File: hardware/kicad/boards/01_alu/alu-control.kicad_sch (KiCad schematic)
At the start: 4 parts, among them U13 74LS08, U14 74HC86

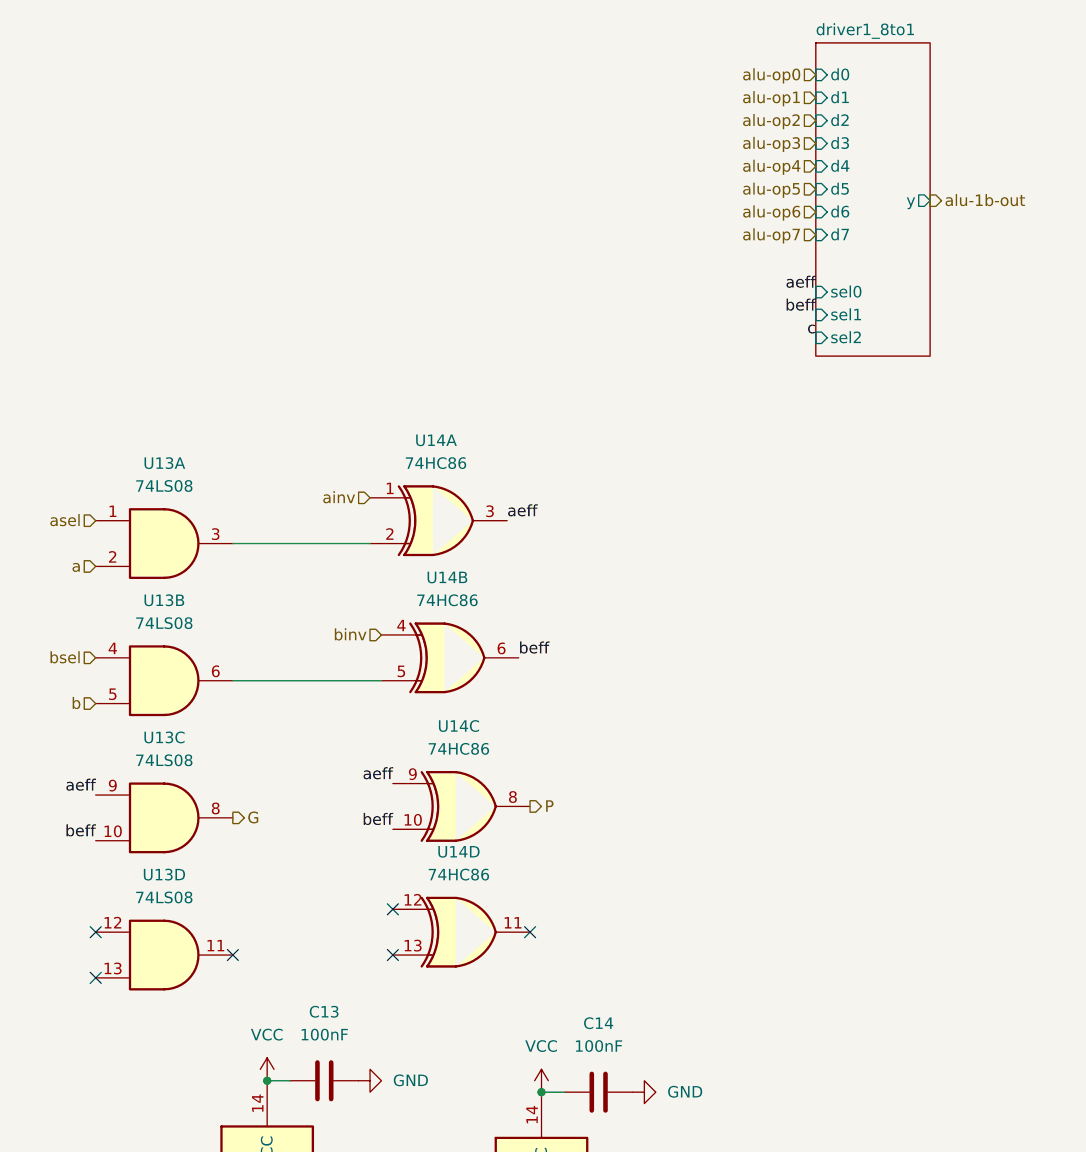
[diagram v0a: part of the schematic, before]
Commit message: schematics: initiated kicad project for all boards to match simulation
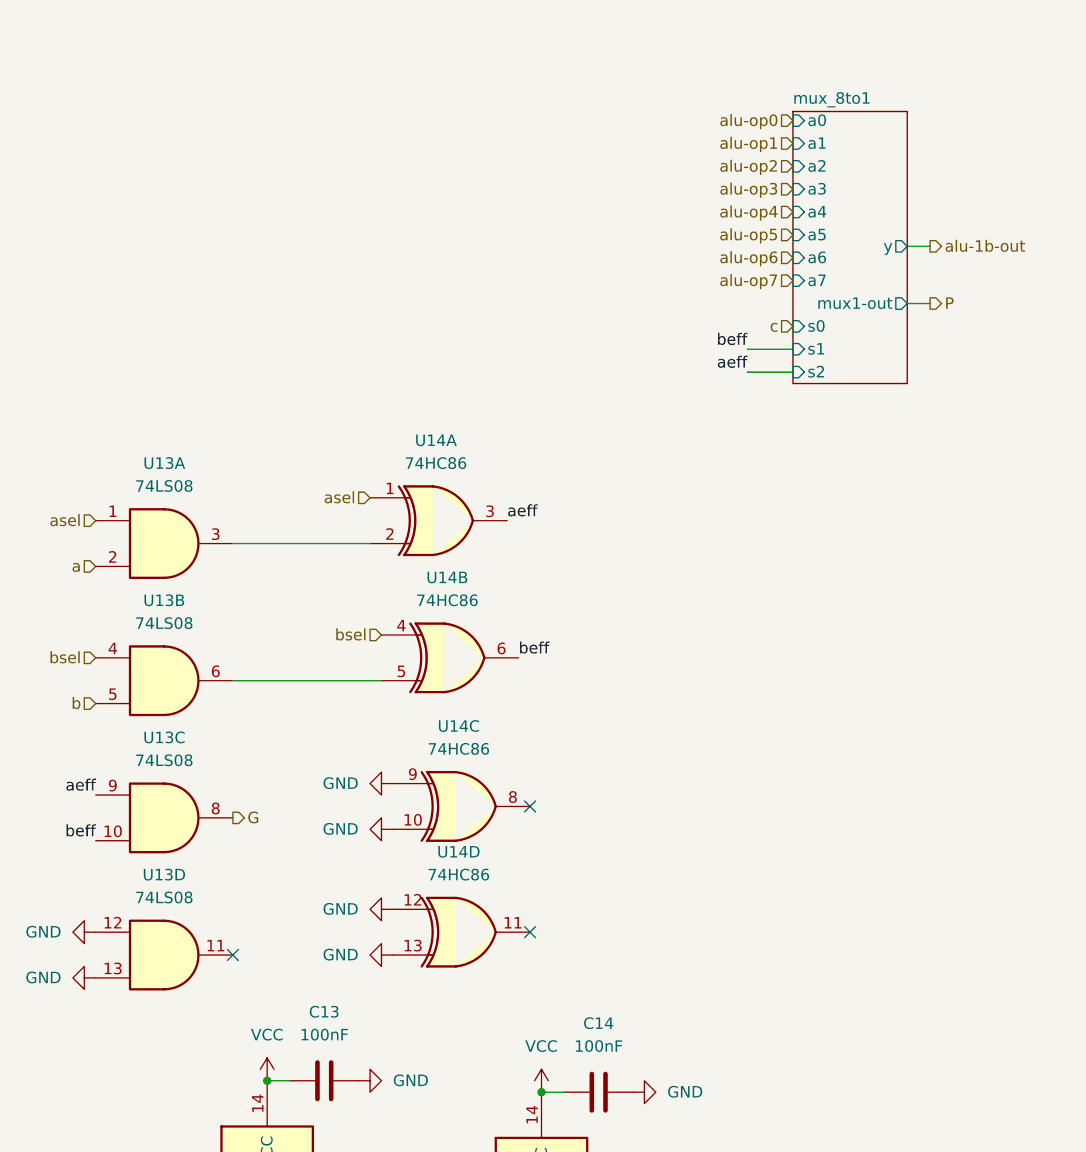
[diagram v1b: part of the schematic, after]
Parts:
- C13, C14: footprint Capacitor_SMD:C_0805_2012Metric -> (none)
- U13, U14: footprint Package_SO:SOIC-14_3.9x8.7mm_P1.27mm -> (none)
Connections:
- net ainv is gone; now on net asel: U14.1
- net binv is gone; now on net bsel: U14.4
- net GND: now also U13.12, U13.13, U14.10, U14.12, U14.13, U14.9
- net P: no longer U14.8
- net aeff: no longer U14.9
- net beff: no longer U14.10
- no-connect marks 6 -> 3
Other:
- removed sheet driver1_8to1
- added sheet mux_8to1 (../../modules/mux/mux_8to1.kicad_sch)

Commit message: feat: designed alu0-control unit and wired on top level of 32b alu
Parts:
- removed C13, C14: 100nF, symbol Device:C
- removed U13: 74LS08, symbol 74xx:74LS08
- removed U14: 74HC86, symbol 74xx:74HC86
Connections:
- no-connect marks 3 -> 0
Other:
- removed sheet mux_8to1

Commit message: kicad: checkpoint; designed the alu display logic; clock circuit
Added registers for each display to ensure robustness and less worry about debugging screen, keeping focus on the alu board and other components
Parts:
- added C1, C2, C3, C4: C, Capacitor_SMD:C_0805_2012Metric, symbol Device:C
- added U1, U2: KM28C64A, Package_DIP:DIP-28_W15.24mm, symbol Memory_EEPROM:KM28C64A
- added U3: 74LS540, Package_SO:SOIC-20W_7.5x12.8mm_P1.27mm, symbol 74xx:74LS540
- added U4: 74AHC541, Package_SO:SOIC-20W_7.5x12.8mm_P1.27mm, symbol 74xx:74AHC541
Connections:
- new net GND: C1.1, C2.1, C3.1, C4.1, U1.14 (GND), U1.2 (A12), U1.20 (~{CE}), U1.21 (A10), U1.22 (~{OE}), U1.23 (A11), U1.27 (~{WE}), U2.14 (GND), U2.2 (A12), U2.20 (~{CE}), U2.21 (A10), U2.22 (~{OE}), U2.23 (A11), U2.27 (~{WE}), U3.1 (G1), U3.10 (GND), U3.19 (G2), U4.1 (G1), U4.10 (GND), U4.19 (G2)
- new net VCC: C1.2, C2.2, C3.2, C4.2, U1.28 (VCC), U2.28 (VCC), U3.20 (VCC), U4.20 (VCC)
- new net ainv: U2.12 (I/O1)
- new net alu-opcode0: U1.11 (I/O0)
- new net alu-opcode1: U1.12 (I/O1)
- new net alu-opcode2: U1.13 (I/O2)
- new net alu-opcode3: U1.15 (I/O3)
- new net alu-opcode4: U1.16 (I/O4)
- new net alu-opcode5: U1.17 (I/O5)
- new net alu-opcode6: U1.18 (I/O6)
- new net alu-opcode7: U1.19 (I/O7)
- new net asel: U2.11 (I/O0)
- new net binv: U2.15 (I/O3)
- new net bsel: U2.13 (I/O2)
- new net csel0: U2.16 (I/O4)
- new net csel1: U2.17 (I/O5)
- new net ir-op0: U3.2 (A0)
- new net ir-op1: U3.3 (A1)
- new net ir-op2: U3.4 (A2)
- new net ir-op3: U3.5 (A3)
- new net ir-op4: U3.6 (A4)
- new net ir-op5: U3.7 (A5)
- new net ir-op6: U3.8 (A6)
- new net ir-op7: U3.9 (A7)
- new net ir-op8: U4.18 (Y0), U4.2 (A0)
- new net ir-op9: U4.17 (Y1), U4.3 (A1)
- new net ir-opcode0: U1.10 (A0), U2.10 (A0), U3.18 (Y0)
- new net ir-opcode1: U1.9 (A1), U2.9 (A1), U3.17 (Y1)
- new net ir-opcode2: U1.8 (A2), U2.8 (A2), U3.16 (Y2)
- new net ir-opcode3: U1.7 (A3), U2.7 (A3), U3.15 (Y3)
- new net ir-opcode4: U1.6 (A4), U2.6 (A4), U3.14 (Y4)
- new net ir-opcode5: U1.5 (A5), U2.5 (A5), U3.13 (Y5)
- new net ir-opcode6: U1.4 (A6), U2.4 (A6), U3.12 (Y6)
- new net ir-opcode7: U1.3 (A7), U2.3 (A7), U3.11 (Y7)
- new net ir-opcode8: U1.25 (A8), U2.25 (A8)
- new net ir-opcode9: U1.24 (A9), U2.24 (A9)
- no-connect marks 0 -> 14

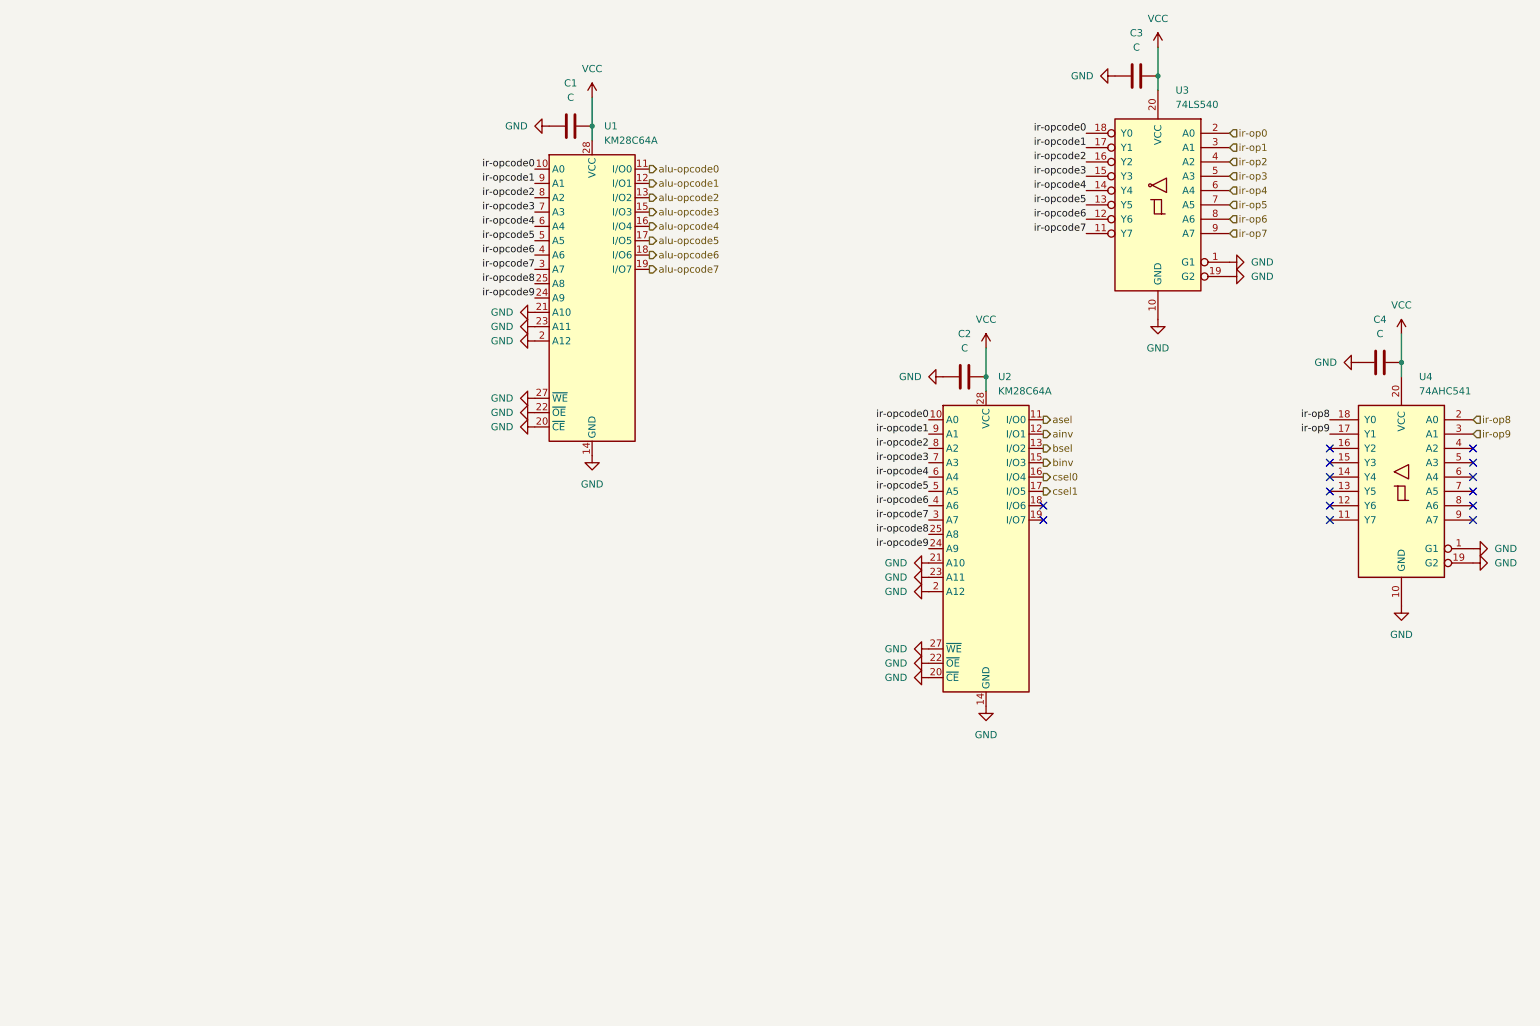
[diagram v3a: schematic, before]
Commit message: fix: fixed erc to 0; remaining are warnings about labeling which are being fixed; latest alu schematics pending decoration and organization
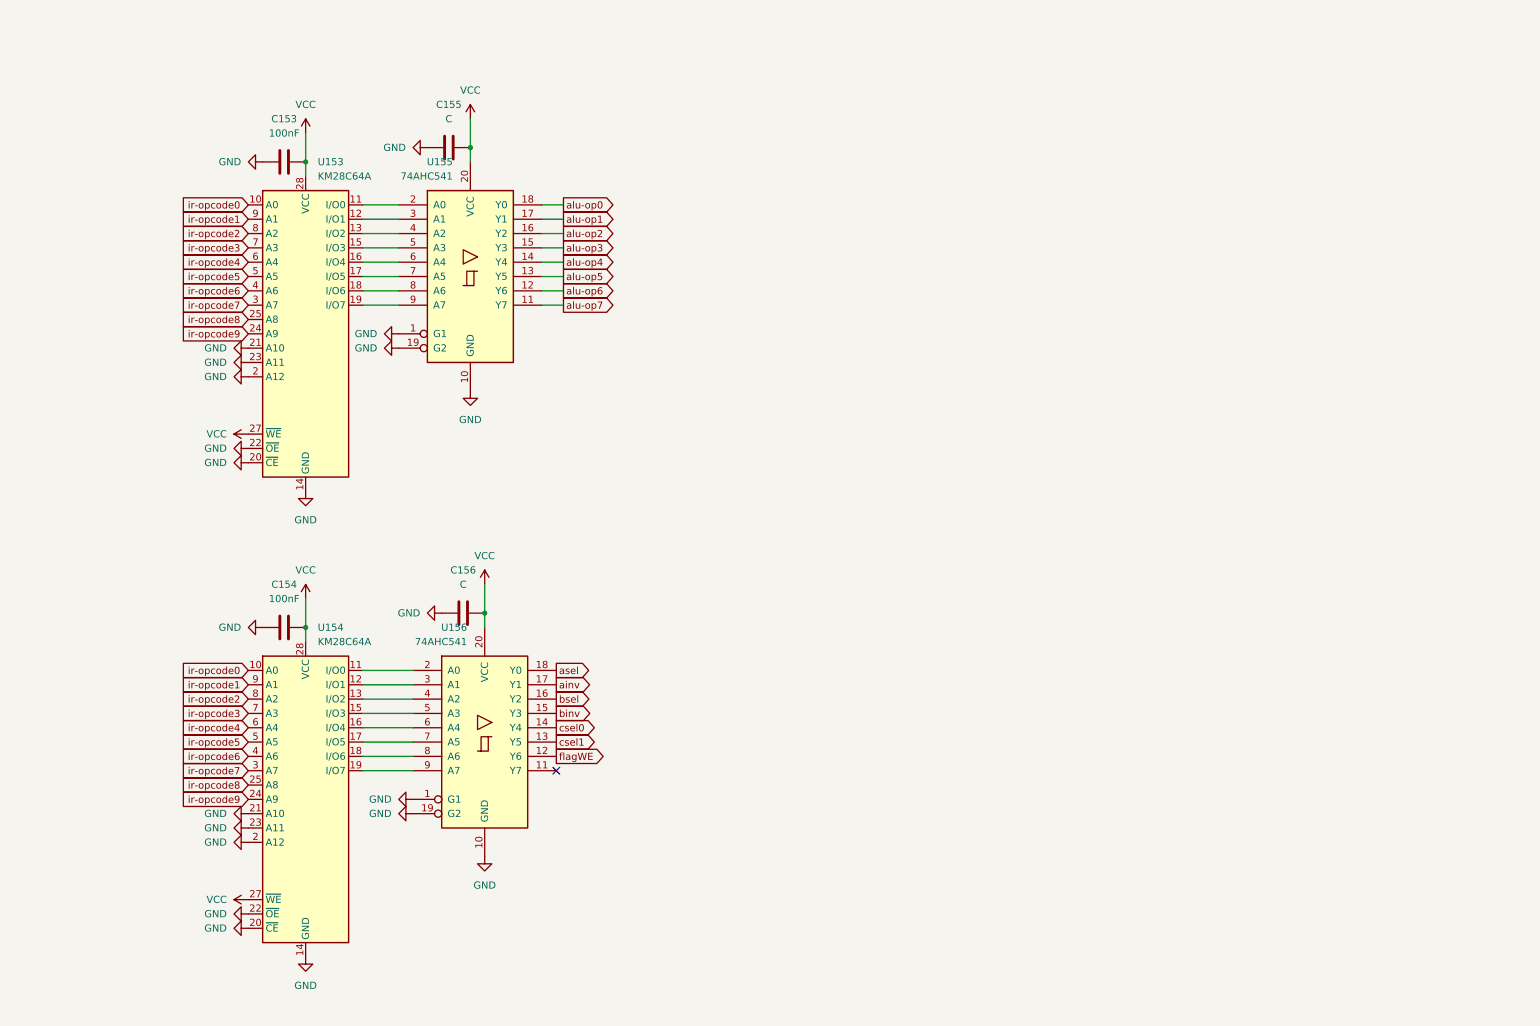
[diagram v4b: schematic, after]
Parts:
- removed C1, C2, C3, C4: C, Capacitor_SMD:C_0805_2012Metric, symbol Device:C
- removed U1, U2: KM28C64A, Package_DIP:DIP-28_W15.24mm, symbol Memory_EEPROM:KM28C64A
- removed U3: 74LS540, Package_SO:SOIC-20W_7.5x12.8mm_P1.27mm, symbol 74xx:74LS540
- removed U4: 74AHC541, Package_SO:SOIC-20W_7.5x12.8mm_P1.27mm, symbol 74xx:74AHC541
- added C153, C154: 100nF, Capacitor_SMD:C_0805_2012Metric, symbol Device:C
- added C155, C156: C, Capacitor_SMD:C_0805_2012Metric, symbol Device:C
- added U153, U154: KM28C64A, Package_DIP:DIP-28_W15.24mm, symbol Memory_EEPROM:KM28C64A
- added U155, U156: 74AHC541, Package_SO:SOIC-20W_7.5x12.8mm_P1.27mm, symbol 74xx:74AHC541
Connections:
- net GND: now also C153.1, C154.1, C155.1, C156.1, U153.14 (GND), U153.2 (A12), U153.20 (~{CE}), U153.21 (A10), U153.22 (~{OE}), U153.23 (A11), U154.14 (GND), U154.2 (A12), U154.20 (~{CE}), U154.21 (A10), U154.22 (~{OE}), U154.23 (A11), U155.1 (G1), U155.10 (GND), U155.19 (G2), U156.1 (G1), U156.10 (GND), U156.19 (G2)
- net VCC: now also C153.2, C154.2, C155.2, C156.2, U153.27 (~{WE}), U153.28 (VCC), U154.27 (~{WE}), U154.28 (VCC), U155.20 (VCC), U156.20 (VCC)
- net ainv: now also U156.17 (Y1)
- net asel: now also U156.18 (Y0)
- net binv: now also U156.15 (Y3)
- net bsel: now also U156.16 (Y2)
- net csel0: now also U156.14 (Y4)
- net csel1: now also U156.13 (Y5)
- net ir-opcode0: now also U153.10 (A0), U154.10 (A0)
- net ir-opcode1: now also U153.9 (A1), U154.9 (A1)
- net ir-opcode2: now also U153.8 (A2), U154.8 (A2)
- net ir-opcode3: now also U153.7 (A3), U154.7 (A3)
- net ir-opcode4: now also U153.6 (A4), U154.6 (A4)
- net ir-opcode5: now also U153.5 (A5), U154.5 (A5)
- net ir-opcode6: now also U153.4 (A6), U154.4 (A6)
- net ir-opcode7: now also U153.3 (A7), U154.3 (A7)
- net ir-opcode8: now also U153.25 (A8), U154.25 (A8)
- net ir-opcode9: now also U153.24 (A9), U154.24 (A9)
- new net: U153.11 (I/O0), U155.2 (A0)
- new net: U153.12 (I/O1), U155.3 (A1)
- new net: U153.13 (I/O2), U155.4 (A2)
- new net: U153.15 (I/O3), U155.5 (A3)
- new net: U153.16 (I/O4), U155.6 (A4)
- new net: U153.17 (I/O5), U155.7 (A5)
- new net: U153.18 (I/O6), U155.8 (A6)
- new net: U153.19 (I/O7), U155.9 (A7)
- new net: U154.11 (I/O0), U156.2 (A0)
- new net: U154.12 (I/O1), U156.3 (A1)
- new net: U154.13 (I/O2), U156.4 (A2)
- new net: U154.15 (I/O3), U156.5 (A3)
- new net: U154.16 (I/O4), U156.6 (A4)
- new net: U154.17 (I/O5), U156.7 (A5)
- new net: U154.18 (I/O6), U156.8 (A6)
- new net: U154.19 (I/O7), U156.9 (A7)
- new net alu-op0: U155.18 (Y0)
- new net alu-op1: U155.17 (Y1)
- new net alu-op2: U155.16 (Y2)
- new net alu-op3: U155.15 (Y3)
- new net alu-op4: U155.14 (Y4)
- new net alu-op5: U155.13 (Y5)
- new net alu-op6: U155.12 (Y6)
- new net alu-op7: U155.11 (Y7)
- new net flagWE: U156.12 (Y6)
- no-connect marks 14 -> 1

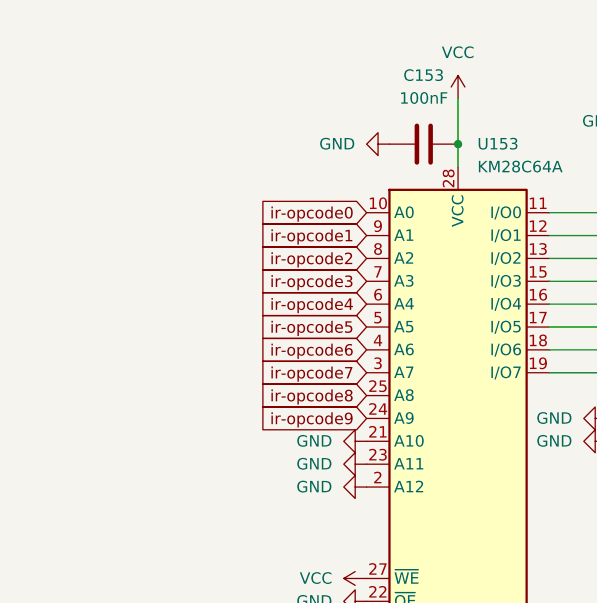
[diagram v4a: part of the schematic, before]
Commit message: refactor: placing buses in design across alu to improve readability and debugging
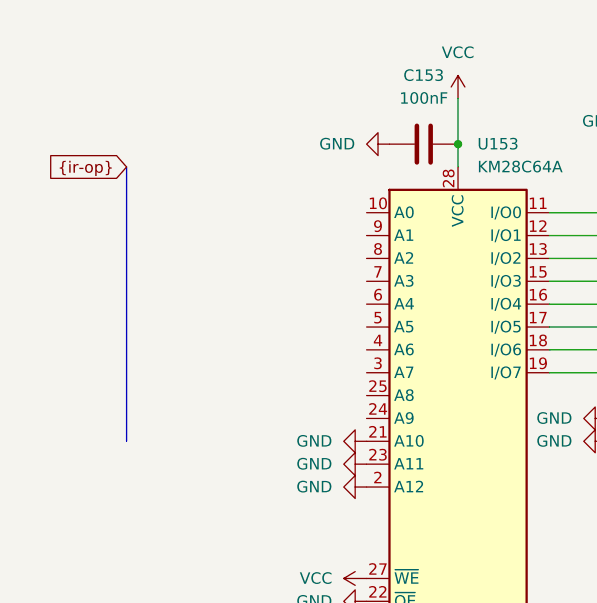
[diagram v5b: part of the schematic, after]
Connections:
- net ir-opcode0: no longer U153.10 (A0)
- net ir-opcode1: no longer U153.9 (A1)
- net ir-opcode2: no longer U153.8 (A2)
- net ir-opcode3: no longer U153.7 (A3)
- net ir-opcode4: no longer U153.6 (A4)
- net ir-opcode5: no longer U153.5 (A5)
- net ir-opcode6: no longer U153.4 (A6)
- net ir-opcode7: no longer U153.3 (A7)
- net ir-opcode8: no longer U153.25 (A8)
- net ir-opcode9: no longer U153.24 (A9)
